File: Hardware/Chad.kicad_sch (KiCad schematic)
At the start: 41 parts, among them J1 RBUS, J2 GPIO Breakout, J3 ServoCH1, J4 ServoCH2, U1 ESP32-S3, Y1 40MHz±10ppm

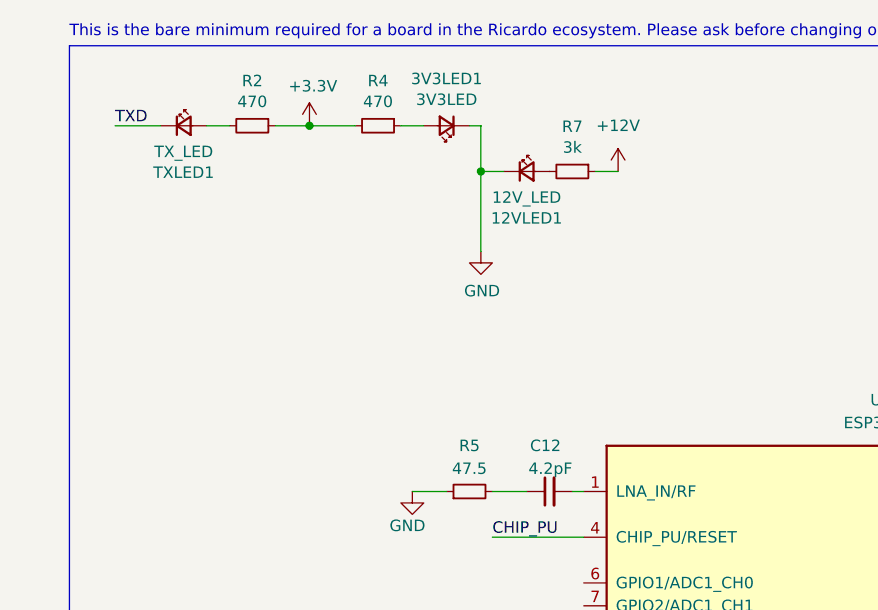
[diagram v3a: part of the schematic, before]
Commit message: all the important stuff routed, only back gfx and via stitch left
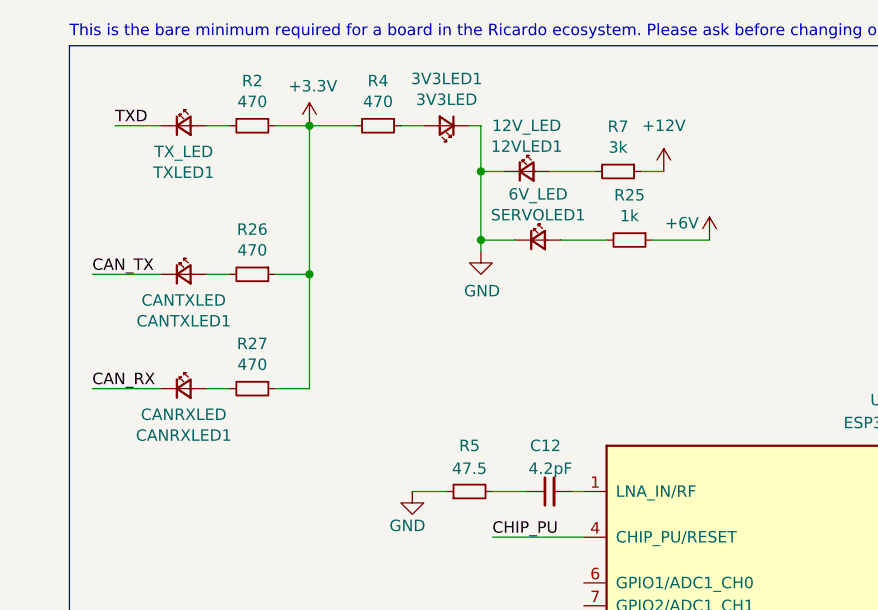
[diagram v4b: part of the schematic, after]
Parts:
- added CANRXLED1: CANRXLED, LED_SMD:LED_0402_1005Metric, symbol Device:LED_Small
- added CANTXLED1: CANTXLED, LED_SMD:LED_0402_1005Metric, symbol Device:LED_Small
- added R25: 1k, Resistor_SMD:R_0402_1005Metric, symbol Device:R_Small
- added R26, R27: 470, Resistor_SMD:R_0402_1005Metric, symbol Device:R_Small
- added SERVOLED1: 6V_LED, LED_SMD:LED_0402_1005Metric, symbol Device:LED_Small
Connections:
- net +3V3: now also R26.1, R27.1
- net +6V: now also R25.1
- net CAN_RX: now also CANRXLED1.1 (K)
- net CAN_TX: now also CANTXLED1.1 (K)
- net GND: now also SERVOLED1.1 (K)
- new net: CANTXLED1.2 (A), R26.2
- new net: R25.2, SERVOLED1.2 (A)
- new net: CANRXLED1.2 (A), R27.2
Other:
- moved on the sheet: R7

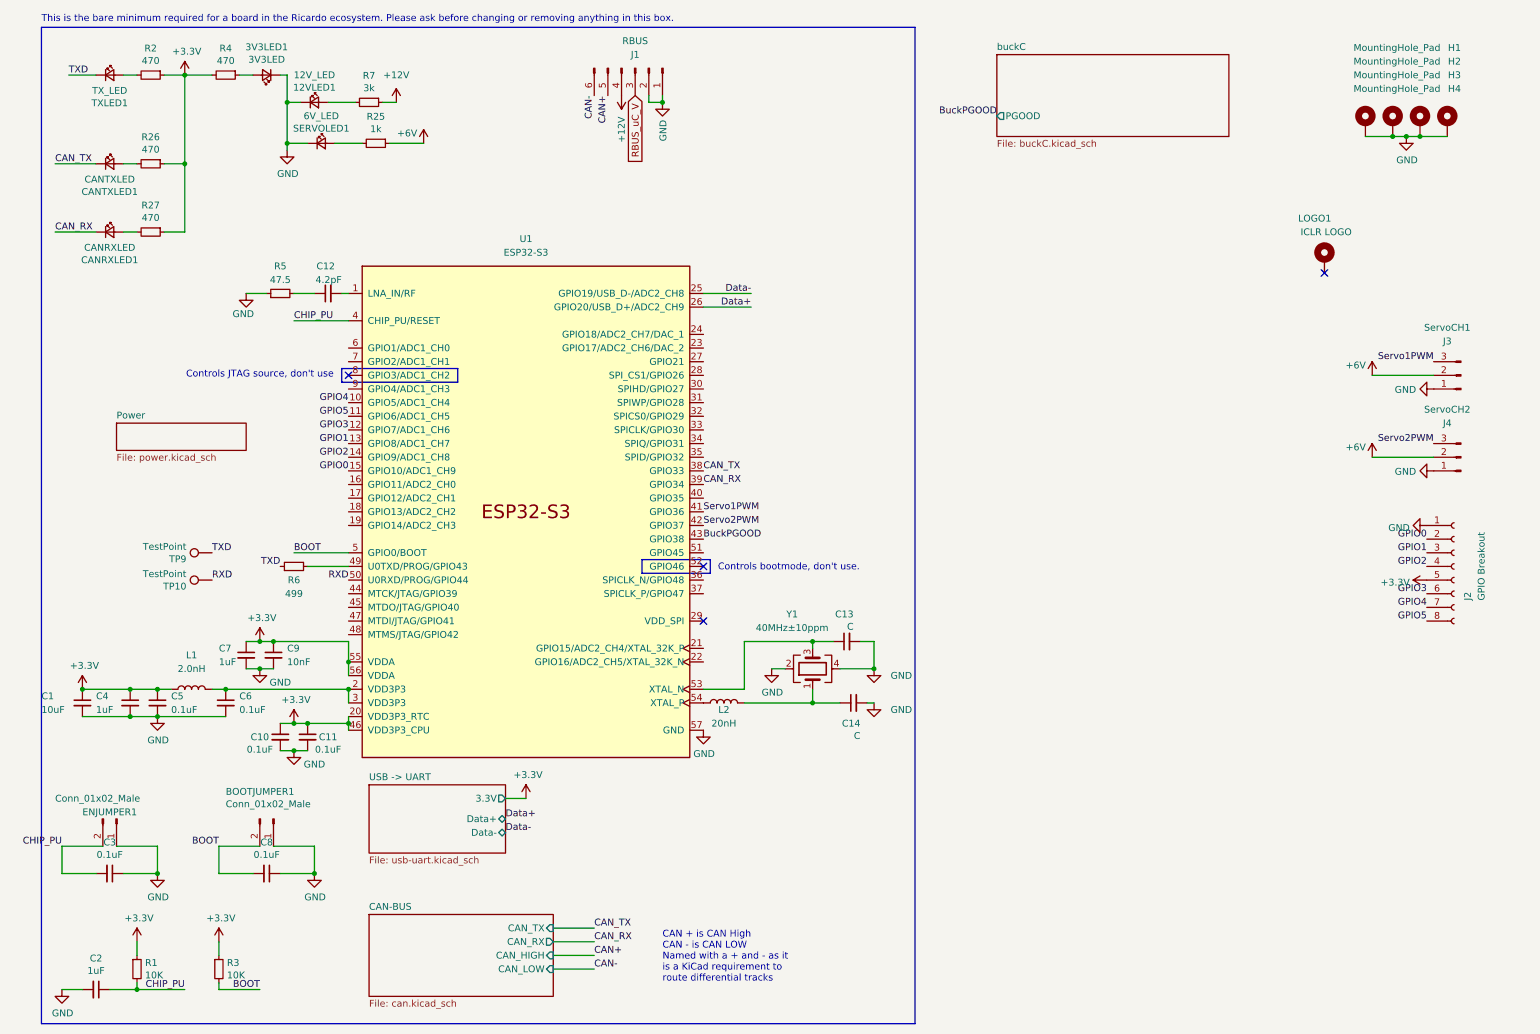
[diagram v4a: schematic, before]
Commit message: fixed via numbers, added gpio pullup option, need to decide PGood flag
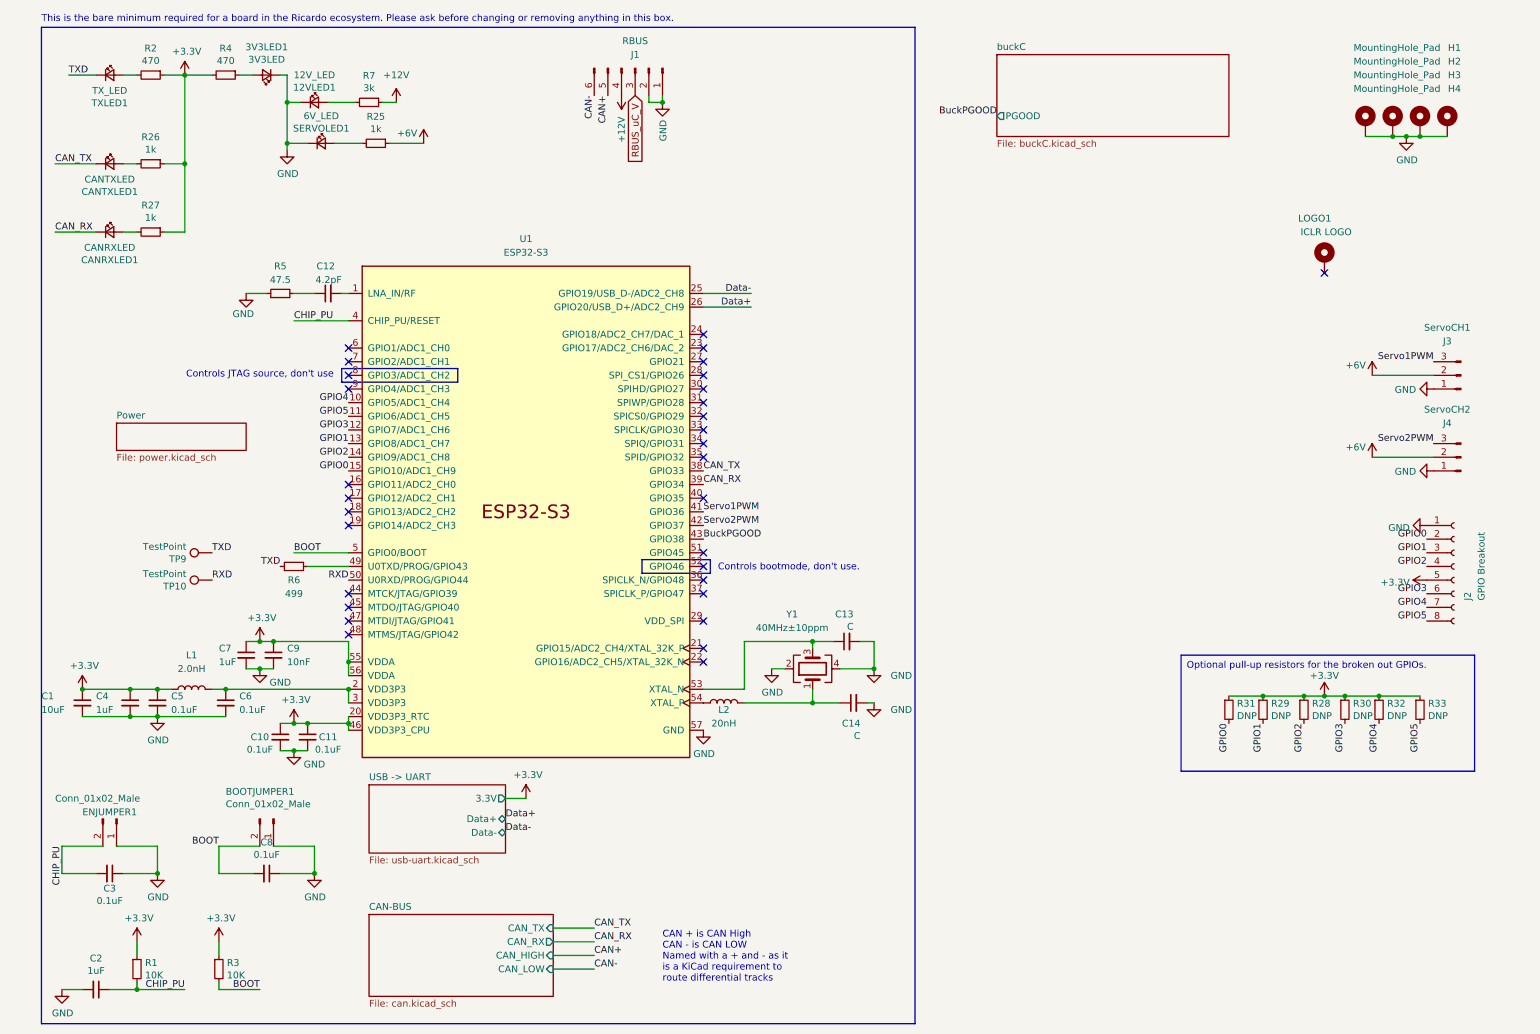
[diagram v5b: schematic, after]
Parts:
- added R28, R29, R30, R31, R32, R33: DNP, Resistor_SMD:R_0402_1005Metric, symbol Device:R_Small
- R26, R27: value 470 -> 1k
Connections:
- net +3V3: now also R28.1, R29.1, R30.1, R31.1, R32.1, R33.1
- net GPIO0: now also R31.2
- net GPIO1: now also R29.2
- net GPIO2: now also R28.2
- net GPIO3: now also R30.2
- net GPIO4: now also R32.2
- net GPIO5: now also R33.2
- no-connect marks 4 -> 31

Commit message: v2 finished? (pre-review)
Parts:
- added R34: 2.2k, Resistor_SMD:R_0402_1005Metric, symbol Device:R_Small
- added R35: 1.5k, Resistor_SMD:R_0402_1005Metric, symbol Device:R_Small
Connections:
- net BuckPGOOD: now also R34.2, R35.1
- net GND: now also R34.1
- new net buckC/PGOOD: R35.2
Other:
- moved on the sheet: LOGO1
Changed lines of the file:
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@@
   (no_connect (at 135.89 87.63))
   (no_connect (at 69.85 97.79))
-  (no_connect (at 251.46 58.42))
+  (no_connect (at 275.59 50.8))
   (no_connect (at 135.89 123.19))
   (no_connect (at 69.85 100.33))
@@
     (stroke (width 0) (type default))
   )
+  (wire (pts (xy 233.68 29.21) (xy 236.22 29.21))
+    (stroke (width 0) (type default))
+  )
   (wire (pts (xy 29.21 135.89) (xy 34.29 135.89))
     (stroke (width 0) (type default))
@@
   )
   (wire (pts (xy 22.86 170.18) (xy 16.51 170.18))
+    (stroke (width 0) (type default))
+  )
+  (wire (pts (xy 236.22 34.29) (xy 236.22 38.1))
     (stroke (width 0) (type default))
   )
@@
     (effects (font (size 1.27 1.27)) (justify right bottom))
   )
+  (label "BuckPGOOD" (at 236.22 36.83 0) (fields_autoplaced)
+    (effects (font (size 1.27 1.27)) (justify left bottom))
+  )
   (label "Servo2PWM" (at 135.89 105.41 0) (fields_autoplaced)
     (effects (font (size 1.27 1.27)) (justify left bottom))
@@
   )
   (label "GPIO0" (at 233.68 142.24 270) (fields_autoplaced)
-    (effects (font (size 1.27 1.27)) (justify right bottom))
-  )
-  (label "BuckPGOOD" (at 190.5 29.21 180) (fields_autoplaced)
     (effects (font (size 1.27 1.27)) (justify right bottom))
   )
@@
     )
   )
+  (symbol (lib_id "Device:R_Small") (at 236.22 31.75 180) (unit 1)
+    (in_bom yes) (on_board yes) (dnp no)
+    (property "Reference" "R35" (at 241.1984 31.75 90)
+      (effects (font (size 1.27 1.27)))
+    )
+    (property "Value" "1.5k" (at 238.887 31.75 90)
+      (effects (font (size 1.27 1.27)))
+    )
+    (property "Footprint" "Resistor_SMD:R_0402_1005Metric" (at 236.22 31.75 0)
+      (effects (font (size 1.27 1.27)) hide)
+    )
+    (property "Datasheet" "~" (at 236.22 31.75 0)
+      (effects (font (size 1.27 1.27)) hide)
+    )
+    (pin "1")
+    (pin "2")
+    (instances
+      (project "Chad"
+        (path "/7db990e4-92e1-4f99-b4d2-435bbec1ba83"
+          (reference "R35") (unit 1)
+        )
+      )
+    )
+  )
   (symbol (lib_id "power:+6V") (at 83.82 34.29 0) (unit 1)
     (in_bom yes) (on_board yes) (dnp no)
@@
     )
   )
-  (symbol (lib_id "Mechanical:MountingHole_Pad") (at 251.46 55.88 0) (unit 1)
-    (in_bom yes) (on_board yes) (dnp no)
-    (property "Reference" "LOGO1" (at 252.73 48.26 0)
+  (symbol (lib_id "Mechanical:MountingHole_Pad") (at 275.59 48.26 0) (unit 1)
+    (in_bom yes) (on_board yes) (dnp no)
+    (property "Reference" "LOGO1" (at 276.86 40.64 0)
       (effects (font (size 1.27 1.27)) (justify right))
     )
-    (property "Value" "ICLR LOGO" (at 256.54 50.8 0)
+    (property "Value" "ICLR LOGO" (at 280.67 43.18 0)
       (effects (font (size 1.27 1.27)) (justify right))
     )
-    (property "Footprint" "iclr:iclr_logo" (at 251.46 55.88 0)
-      (effects (font (size 1.27 1.27)) hide)
-    )
-    (property "Datasheet" "~" (at 251.46 55.88 0)
+    (property "Footprint" "iclr:iclr_logo" (at 275.59 48.26 0)
+      (effects (font (size 1.27 1.27)) hide)
+    )
+    (property "Datasheet" "~" (at 275.59 48.26 0)
       (effects (font (size 1.27 1.27)) hide)
     )
@@
         (path "/7db990e4-92e1-4f99-b4d2-435bbec1ba83"
           (reference "R25") (unit 1)
+        )
+      )
+    )
+  )
+  (symbol (lib_id "Device:R_Small") (at 236.22 40.64 180) (unit 1)
+    (in_bom yes) (on_board yes) (dnp no)
+    (property "Reference" "R34" (at 241.1984 40.64 90)
+      (effects (font (size 1.27 1.27)))
+    )
+    (property "Value" "2.2k" (at 238.887 40.64 90)
+      (effects (font (size 1.27 1.27)))
+    )
+    (property "Footprint" "Resistor_SMD:R_0402_1005Metric" (at 236.22 40.64 0)
+      (effects (font (size 1.27 1.27)) hide)
+    )
+    (property "Datasheet" "~" (at 236.22 40.64 0)
+      (effects (font (size 1.27 1.27)) hide)
+    )
+    (pin "1")
+    (pin "2")
+    (instances
+      (project "Chad"
+        (path "/7db990e4-92e1-4f99-b4d2-435bbec1ba83"
+          (reference "R34") (unit 1)
         )
       )
@@
     )
   )
+  (symbol (lib_id "power:GND") (at 236.22 43.18 0) (unit 1)
+    (in_bom yes) (on_board yes) (dnp no)
+    (property "Reference" "#PWR081" (at 236.22 49.53 0)
+      (effects (font (size 1.27 1.27)) hide)
+    )
+    (property "Value" "GND" (at 236.347 47.5742 0)
+      (effects (font (size 1.27 1.27)))
+    )
+    (property "Footprint" "" (at 236.22 43.18 0)
+      (effects (font (size 1.27 1.27)) hide)
+    )
+    (property "Datasheet" "" (at 236.22 43.18 0)
+      (effects (font (size 1.27 1.27)) hide)
+    )
+    (pin "1")
+    (instances
+      (project "Chad"
+        (path "/7db990e4-92e1-4f99-b4d2-435bbec1ba83"
+          (reference "#PWR081") (unit 1)
+        )
+      )
+    )
+  )
   (symbol (lib_id "Device:R_Small") (at 240.03 139.7 0) (unit 1)
     (in_bom yes) (on_board yes) (dnp no)
@@
       (effects (font (size 1.27 1.27)) (justify left top))
     )
-    (pin "PGOOD" output (at 190.5 29.21 180)
-      (effects (font (size 1.27 1.27)) (justify left))
-    )
-    (instances
+    (pin "PGOOD" output (at 233.68 29.21 0)
+      (effects (font (size 1.27 1.27)) (justify right))
+    )
+    (instances

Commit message: better ICLR logo, 3d model exports with edge connectors
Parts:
- LOGO1: footprint iclr:iclr_logo -> iclr:iclr_logo_estd2018_10mm
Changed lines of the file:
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@@
       (effects (font (size 1.27 1.27)) (justify right))
     )
-    (property "Footprint" "iclr:iclr_logo" (at 275.59 48.26 0)
+    (property "Footprint" "iclr:iclr_logo_estd2018_10mm" (at 275.59 48.26 0)
       (effects (font (size 1.27 1.27)) hide)
     )

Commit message: review changes + some new features
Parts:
- added C45: 0.1uF, Capacitor_SMD:C_0402_1005Metric, symbol Device:C_Small
- added R36: 1.5k, Resistor_SMD:R_0402_1005Metric, symbol Device:R_Small
- added R37: 470, Resistor_SMD:R_0402_1005Metric, symbol Device:R_Small
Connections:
- net +6V: now also C45.1, R36.2
- net BuckPGOOD: now also U1.37 (SPICLK_P/GPIO47); no longer U1.43 (GPIO38)
- net GND: now also R37.1
- net ServoV_LOG: now reaches U1.9 (GPIO4/ADC1_CH3)
- net ServoV_LOG: now also C45.2, R36.1, R37.2
- new net BUCK_EN: U1.43 (GPIO38)
- no-connect marks 31 -> 29
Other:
- sheet buckC ports: added BUCK_EN; removed none
- note removed: "This is the bare minimum required for a board in the Ricardo ecosystem. Please ask before changing or removing anything in this box."
- company: (none) -> Imperial College London Rocketry (ICLR)
- title: (none) -> C.H.A.D
